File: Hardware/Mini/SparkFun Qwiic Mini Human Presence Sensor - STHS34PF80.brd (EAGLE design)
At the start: 25.4 x 12.7 mm, 41 parts, among them J1 Qwiic, J2 Qwiic, U2 STHS34PF80

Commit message: Layout Updates
Finished updates to layout - almost ready for design review
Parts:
- moved LOGO5 33.0 mm to (36.8, 50.8)
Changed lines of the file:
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@@
 <layer number="37" name="tTest" color="7" fill="1" visible="no" active="yes"/>
 <layer number="38" name="bTest" color="7" fill="1" visible="no" active="yes"/>
-<layer number="39" name="tKeepout" color="4" fill="11" visible="yes" active="yes"/>
-<layer number="40" name="bKeepout" color="1" fill="11" visible="yes" active="yes"/>
-<layer number="41" name="tRestrict" color="4" fill="10" visible="yes" active="yes"/>
-<layer number="42" name="bRestrict" color="1" fill="10" visible="yes" active="yes"/>
+<layer number="39" name="tKeepout" color="4" fill="11" visible="no" active="yes"/>
+<layer number="40" name="bKeepout" color="1" fill="11" visible="no" active="yes"/>
+<layer number="41" name="tRestrict" color="4" fill="10" visible="no" active="yes"/>
+<layer number="42" name="bRestrict" color="1" fill="10" visible="no" active="yes"/>
 <layer number="43" name="vRestrict" color="2" fill="10" visible="no" active="yes"/>
 <layer number="44" name="Drills" color="7" fill="1" visible="no" active="yes"/>
@@
 <element name="JP5" library="SparkFun-Aesthetics" package="FIDUCIAL-MICRO" value="FIDUCIALUFIDUCIAL" x="24.765" y="12.065" smashed="yes" rot="MR0"/>
 <element name="JP6" library="SparkFun-Aesthetics" package="FIDUCIAL-MICRO" value="FIDUCIALUFIDUCIAL" x="24.511" y="10.414" smashed="yes"/>
-<element name="LOGO5" library="SparkFun-Aesthetics" package="ORDERING_INSTRUCTIONS" value="SPECIAL_INSTRUCTIONS-ORDERING" x="69.85" y="49.53" smashed="yes"/>
+<element name="LOGO5" library="SparkFun-Aesthetics" package="ORDERING_INSTRUCTIONS" value="SPECIAL_INSTRUCTIONS-ORDERING" x="36.83" y="50.8" smashed="yes"/>
 <element name="J1" library="SparkFun-Connectors" package="JST04_1MM_RA" value="Qwiic" x="5.08" y="8.89" locked="yes" smashed="yes" rot="R270">
 <attribute name="NAME" x="2.921" y="10.287" locked="yes" size="0.6096" layer="25" font="vector" ratio="20" rot="R270"/>

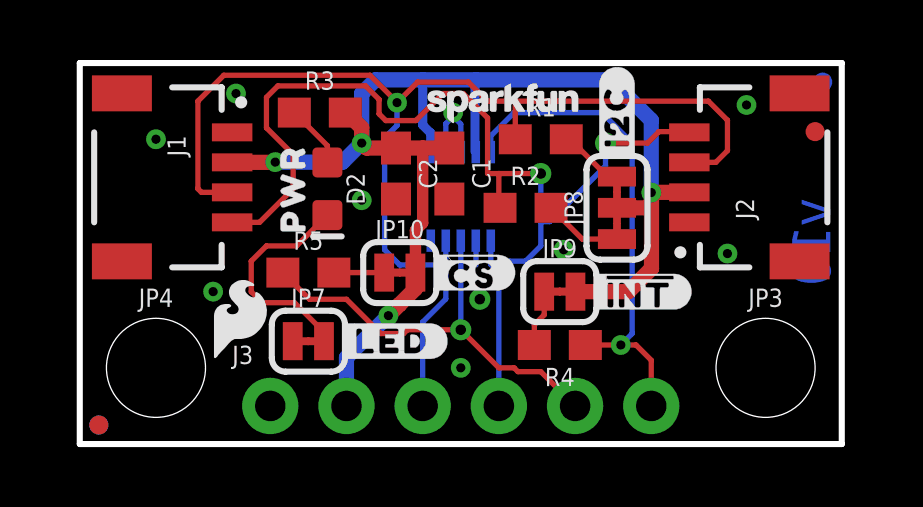
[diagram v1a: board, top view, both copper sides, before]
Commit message: Updated design for review and added production files for Mini
MINI ONLY: Completed layout and worked through design errors, panelized the board, and then created Gerbers for production. Added more comments throughout layout and schematic.
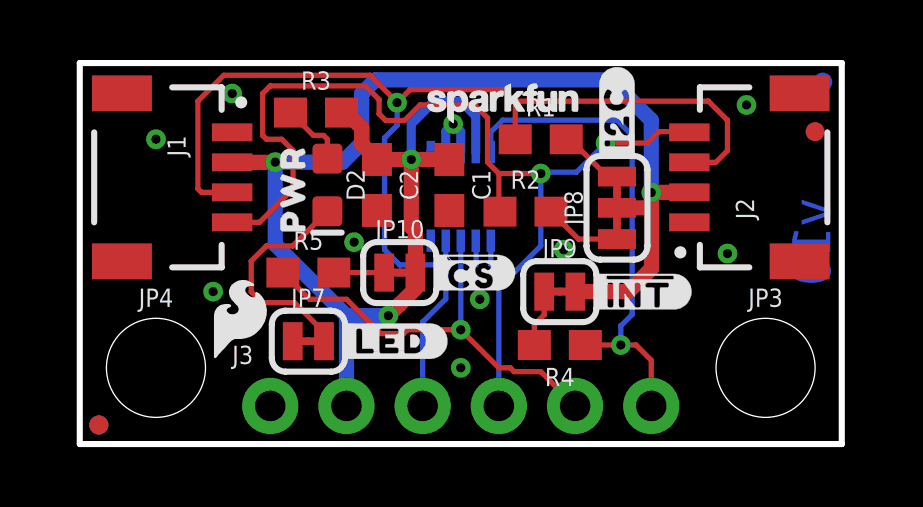
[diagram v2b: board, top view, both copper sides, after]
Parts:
- moved C2 0.74 mm to (9.91, 8.64)
- moved C1 0.38 mm to (12.3, 8.64)
- moved R2 0.13 mm to (14.9, 7.75)
- moved R3 0.13 mm to (7.87, 11.0)
- moved D2 0.13 mm to (8.26, 8.64)
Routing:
- net 3.3V: track 46.2 -> 54.0 mm
- net SCL: track 36.2 -> 35.2 mm
- net GND: track 3.53 -> 2.90 mm
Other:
- board text added: "Solder Mask: Red Thickness: 1.6mm Two layer design Finish: HASL Lead-Free Copper Weight: 1oz Material: TG135-140"

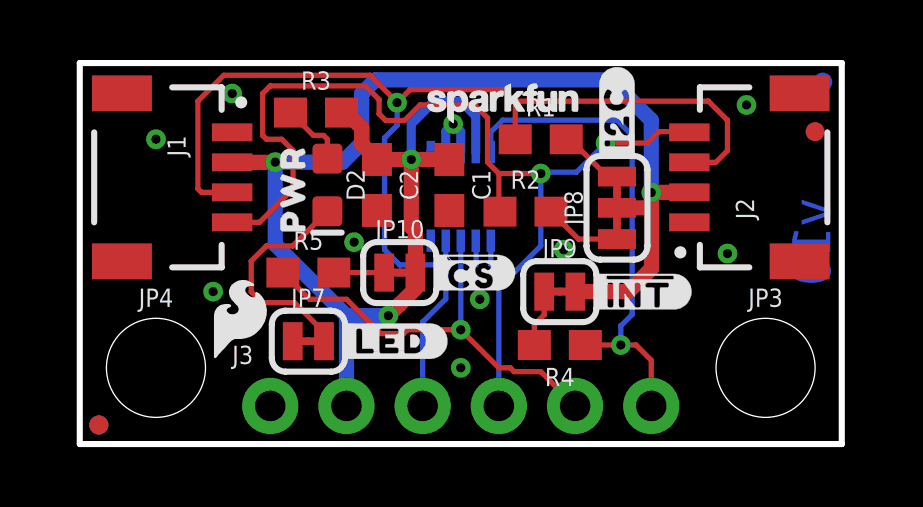
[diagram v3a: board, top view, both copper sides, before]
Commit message: Updated files for design review
Changed ST part to have 80% solder cream; changed panels to be 6x6 boards; changed vector font issues in schematic; added measures; added some more silk for easier part identification
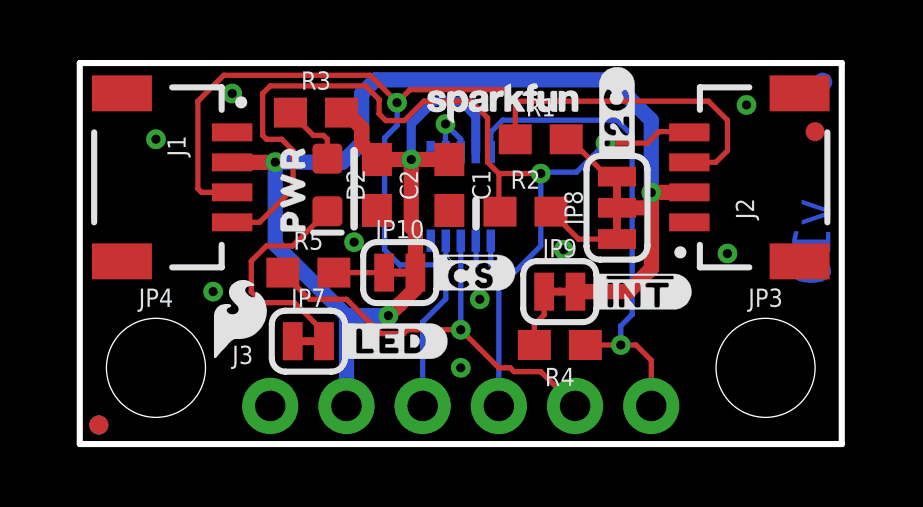
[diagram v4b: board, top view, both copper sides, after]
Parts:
- moved FRAME1 5.68 mm to (-1.27, -26.7)
- renumbered U2 to U1

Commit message: Changed from Qwiic horizontal to qwiic vertical
Changed to the Qwiic Vertical connector we have for a better surface mounting option for the user. Updated the gerbers and panel to now have the correct information
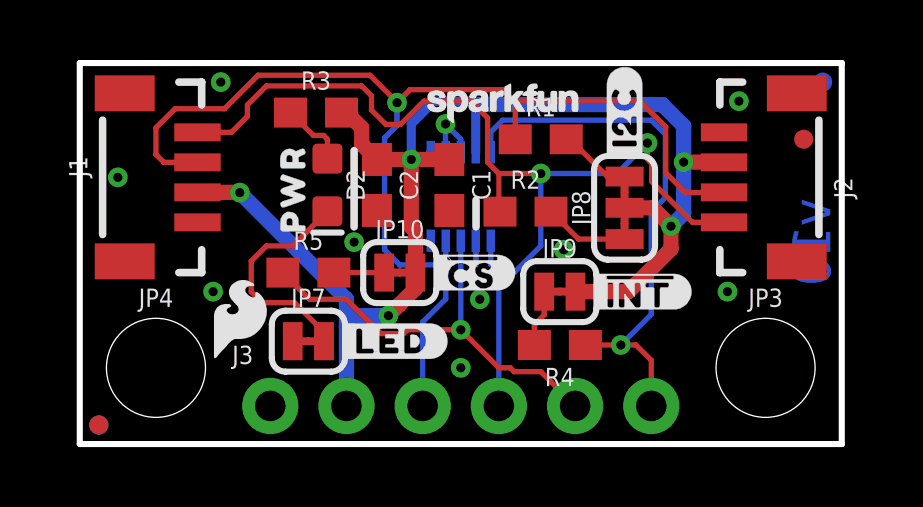
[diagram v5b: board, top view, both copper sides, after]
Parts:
- J1, J2: value Qwiic -> Vertical Qwiic Connector; device SparkFun-Connectors:JST04_1MM_RA -> SparkFun-Connectors:JST04_1MM_VERT
- moved LOGO1 1.27 mm to (21.6, 5.08)
- moved JP6 0.46 mm to (24.1, 10.2)
- moved J1 0.38 mm to (4.70, 8.89), turned to 90 degrees
- moved J2 0.38 mm to (20.7, 8.89), turned to 270 degrees
- moved JP8 0.25 mm to (18.2, 7.87)
- moved U$8 0.25 mm to (18.2, 10.9)
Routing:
- net 3.3V: track 54.0 -> 46.2 mm, vias 4 -> 5
- net INT: track 16.8 -> 18.4 mm
- net SDA: track 40.0 -> 39.4 mm
- net SCL: track 35.3 -> 34.7 mm

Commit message: Small documentation additions
Added I2C address to schematic and units for measures (measures in inches)
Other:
- board text added: "Units in inches"
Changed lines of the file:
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@@
 <drawing>
 <settings>
-<setting alwaysvectorfont="yes"/>
+<setting alwaysvectorfont="no"/>
 <setting verticaltext="up"/>
 </settings>
@@
 <layer number="23" name="tOrigins" color="15" fill="1" visible="yes" active="yes"/>
 <layer number="24" name="bOrigins" color="15" fill="1" visible="yes" active="yes"/>
-<layer number="25" name="tNames" color="7" fill="1" visible="yes" active="yes"/>
-<layer number="26" name="bNames" color="7" fill="1" visible="yes" active="yes"/>
-<layer number="27" name="tValues" color="7" fill="1" visible="yes" active="yes"/>
-<layer number="28" name="bValues" color="7" fill="1" visible="yes" active="yes"/>
-<layer number="29" name="tStop" color="7" fill="3" visible="yes" active="yes"/>
-<layer number="30" name="bStop" color="7" fill="6" visible="yes" active="yes"/>
-<layer number="31" name="tCream" color="7" fill="4" visible="yes" active="yes"/>
-<layer number="32" name="bCream" color="7" fill="5" visible="yes" active="yes"/>
-<layer number="33" name="tFinish" color="6" fill="3" visible="yes" active="yes"/>
-<layer number="34" name="bFinish" color="6" fill="6" visible="yes" active="yes"/>
-<layer number="35" name="tGlue" color="7" fill="4" visible="yes" active="yes"/>
-<layer number="36" name="bGlue" color="7" fill="5" visible="yes" active="yes"/>
-<layer number="37" name="tTest" color="7" fill="1" visible="yes" active="yes"/>
-<layer number="38" name="bTest" color="7" fill="1" visible="yes" active="yes"/>
-<layer number="39" name="tKeepout" color="4" fill="11" visible="yes" active="yes"/>
-<layer number="40" name="bKeepout" color="1" fill="11" visible="yes" active="yes"/>
-<layer number="41" name="tRestrict" color="4" fill="10" visible="yes" active="yes"/>
-<layer number="42" name="bRestrict" color="1" fill="10" visible="yes" active="yes"/>
-<layer number="43" name="vRestrict" color="2" fill="10" visible="yes" active="yes"/>
-<layer number="44" name="Drills" color="7" fill="1" visible="yes" active="yes"/>
+<layer number="25" name="tNames" color="7" fill="1" visible="no" active="yes"/>
+<layer number="26" name="bNames" color="7" fill="1" visible="no" active="yes"/>
+<layer number="27" name="tValues" color="7" fill="1" visible="no" active="yes"/>
+<layer number="28" name="bValues" color="7" fill="1" visible="no" active="yes"/>
+<layer number="29" name="tStop" color="7" fill="3" visible="no" active="yes"/>
+<layer number="30" name="bStop" color="7" fill="6" visible="no" active="yes"/>
+<layer number="31" name="tCream" color="7" fill="4" visible="no" active="yes"/>
+<layer number="32" name="bCream" color="7" fill="5" visible="no" active="yes"/>
+<layer number="33" name="tFinish" color="6" fill="3" visible="no" active="yes"/>
+<layer number="34" name="bFinish" color="6" fill="6" visible="no" active="yes"/>
+<layer number="35" name="tGlue" color="7" fill="4" visible="no" active="yes"/>
+<layer number="36" name="bGlue" color="7" fill="5" visible="no" active="yes"/>
+<layer number="37" name="tTest" color="7" fill="1" visible="no" active="yes"/>
+<layer number="38" name="bTest" color="7" fill="1" visible="no" active="yes"/>
+<layer number="39" name="tKeepout" color="4" fill="11" visible="no" active="yes"/>
+<layer number="40" name="bKeepout" color="1" fill="11" visible="no" active="yes"/>
+<layer number="41" name="tRestrict" color="4" fill="10" visible="no" active="yes"/>
+<layer number="42" name="bRestrict" color="1" fill="10" visible="no" active="yes"/>
+<layer number="43" name="vRestrict" color="2" fill="10" visible="no" active="yes"/>
+<layer number="44" name="Drills" color="7" fill="1" visible="no" active="yes"/>
 <layer number="45" name="Holes" color="7" fill="1" visible="yes" active="yes"/>
-<layer number="46" name="Milling" color="3" fill="1" visible="yes" active="yes"/>
+<layer number="46" name="Milling" color="3" fill="1" visible="no" active="yes"/>
 <layer number="47" name="Measures" color="7" fill="1" visible="yes" active="yes"/>
-<layer number="48" name="Document" color="7" fill="1" visible="yes" active="yes"/>
-<layer number="49" name="Reference" color="7" fill="1" visible="yes" active="yes"/>
+<layer number="48" name="Document" color="7" fill="1" visible="no" active="yes"/>
+<layer number="49" name="Reference" color="7" fill="1" visible="no" active="yes"/>
 <layer number="50" name="dxf" color="7" fill="1" visible="no" active="no"/>
 <layer number="51" name="tDocu" color="6" fill="1" visible="yes" active="yes"/>
-<layer number="52" name="bDocu" color="7" fill="1" visible="yes" active="yes"/>
+<layer number="52" name="bDocu" color="7" fill="1" visible="no" active="yes"/>
 <layer number="53" name="tGND_GNDA" color="7" fill="9" visible="no" active="no"/>
 <layer number="54" name="bGND_GNDA" color="1" fill="9" visible="no" active="no"/>
@@
 <dimension x1="4.699" y1="8.89" x2="4.699" y2="0" x3="-2.54" y3="4.445" textsize="1.778" textratio="15" layer="47" unit="inch"/>
 <dimension x1="4.699" y1="8.89" x2="0" y2="8.89" x3="2.3495" y3="19.05" textsize="1.778" textratio="15" layer="47" unit="inch"/>
+<text x="-15.24" y="-7.62" size="1.27" layer="47" font="vector" ratio="15">Units in inches</text>
 </plain>
 <attributes>

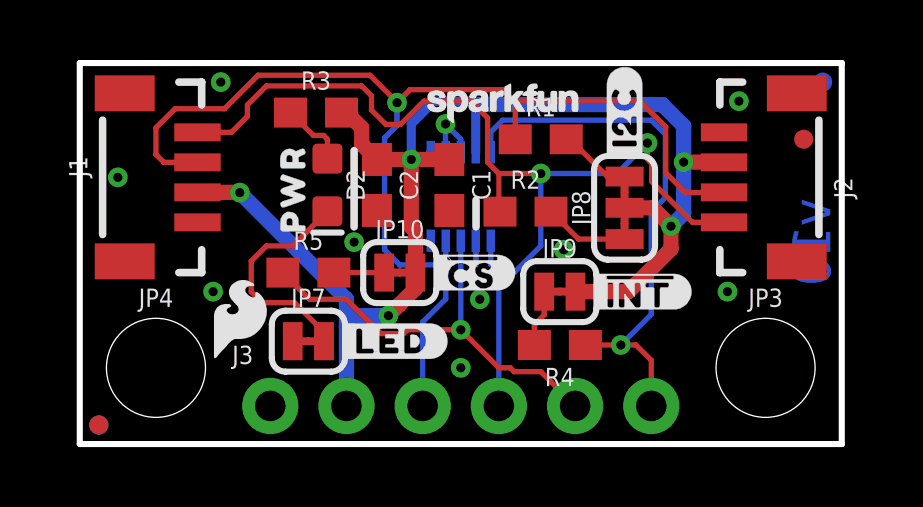
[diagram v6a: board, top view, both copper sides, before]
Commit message: Update to Mini board
Changed silkscreen on the back to have the correct part number on it
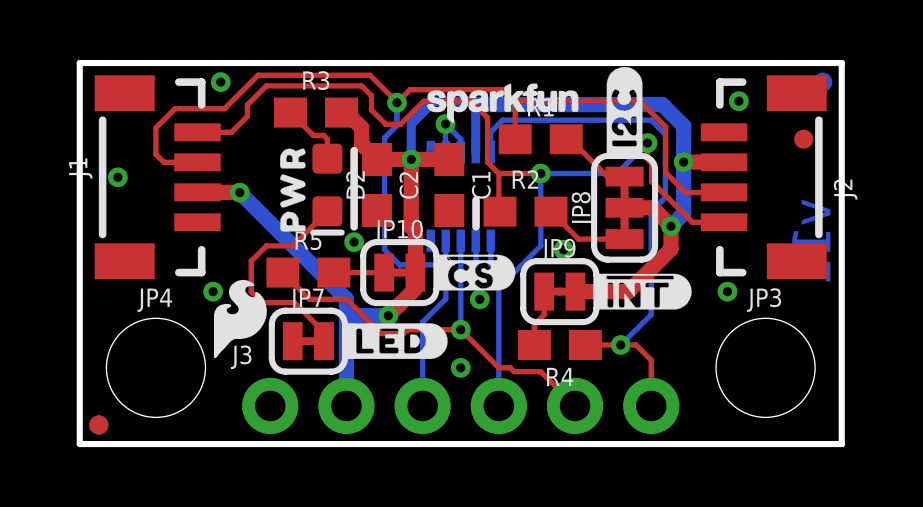
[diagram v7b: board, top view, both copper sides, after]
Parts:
- removed U$12: (no value), output:STH34PF80_PRESENCE_SENSOR10
- added U$6: (no value), output:STHS34PF80_PRESENCE_SENSOR35
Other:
- board text added: "v11"
- board text removed: "v10"
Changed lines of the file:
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@@
 <drawing>
 <settings>
-<setting alwaysvectorfont="no"/>
+<setting alwaysvectorfont="yes"/>
 <setting verticaltext="up"/>
 </settings>
@@
 <layer number="45" name="Holes" color="7" fill="1" visible="yes" active="yes"/>
 <layer number="46" name="Milling" color="3" fill="1" visible="no" active="yes"/>
-<layer number="47" name="Measures" color="7" fill="1" visible="yes" active="yes"/>
+<layer number="47" name="Measures" color="7" fill="1" visible="no" active="yes"/>
 <layer number="48" name="Document" color="7" fill="1" visible="no" active="yes"/>
 <layer number="49" name="Reference" color="7" fill="1" visible="no" active="yes"/>
@@
 <wire x1="0" y1="12.7" x2="0" y2="0" width="0.2032" layer="20"/>
 <text x="25.4" y="-26.67" size="1.778" layer="51" font="vector">M. Chodikov</text>
-<text x="24.384" y="6.731" size="1.27" layer="16" font="vector" ratio="15" rot="SMR270" align="center">v10</text>
+<text x="24.384" y="6.731" size="1.27" layer="16" font="vector" ratio="15" rot="SMR270" align="center">v11</text>
 <rectangle x1="10.414" y1="6.477" x2="14.986" y2="10.033" layer="40"/>
 <rectangle x1="10.414" y1="6.477" x2="14.986" y2="10.033" layer="42"/>
@@
 <element name="U$10" library="output" package="#LED#8" value="" x="10.414" y="3.429" smashed="yes"/>
 <element name="U$11" library="output" package="##INT#9" value="" x="18.669" y="5.08" smashed="yes"/>
-<element name="U$12" library="output" package="STH34PF80_PRESENCE_SENSOR10" value="" x="11.43" y="11.43" smashed="yes" rot="MR0"/>
 <element name="U$13" library="output" package="#GND#35" value="" x="6.35" y="3.81" smashed="yes" rot="MR90"/>
 <element name="U$1" library="output" package="#3V3#36" value="" x="8.89" y="3.81" smashed="yes" rot="MR90"/>
@@
 <attribute name="VALUE" x="23.241" y="8.89" size="0.6096" layer="27" font="vector" rot="R270"/>
 </element>
+<element name="U$6" library="output" package="STHS34PF80_PRESENCE_SENSOR35" value="" x="11.43" y="11.43" smashed="yes" rot="MR0"/>
 </elements>
 <signals>
